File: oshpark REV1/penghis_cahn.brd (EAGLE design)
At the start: 99.4 x 99.6 mm, 67 parts, among them IC1 PCF8574T, P0 TPB1,27, P1 TPB1,27, T1 BC847, T2 BC847, U1 MCP73831

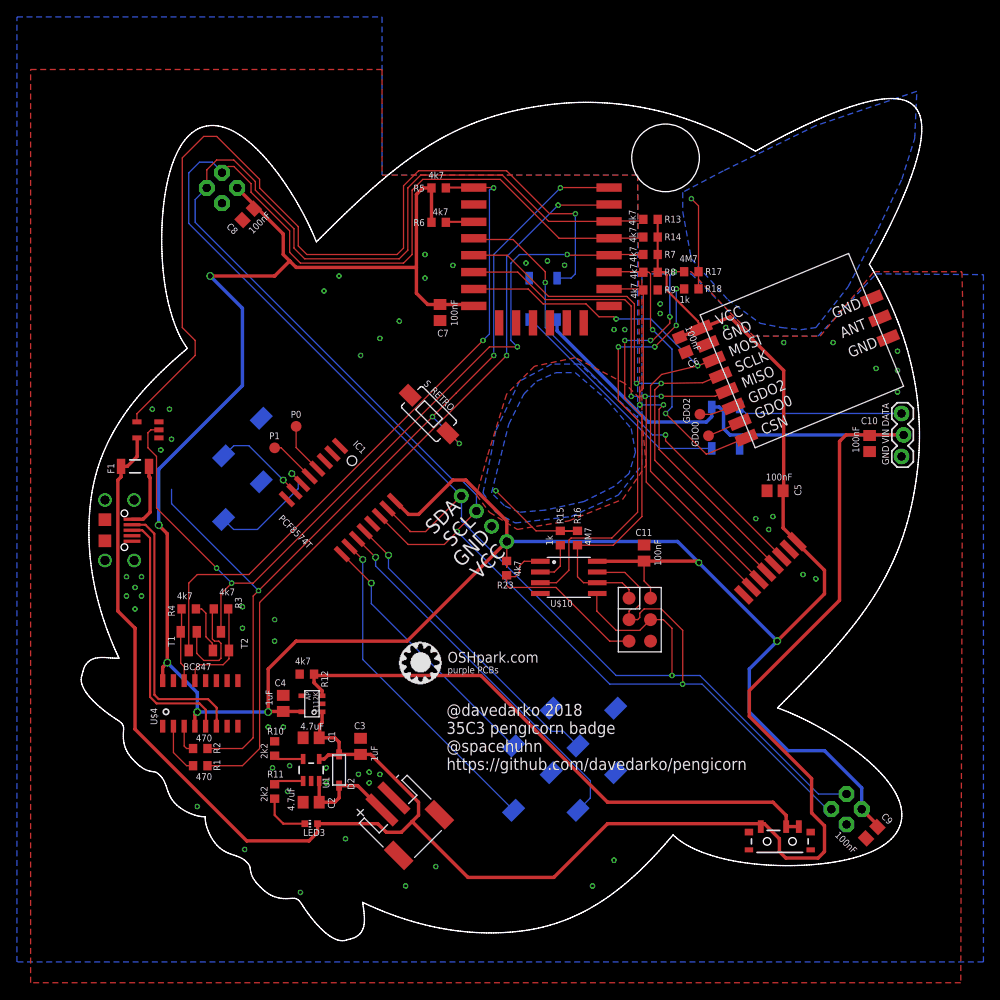
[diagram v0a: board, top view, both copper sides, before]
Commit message: minor updates
added TPS22918 for neopixels
updated labels
moved in nrf24 module
added SAO V1.69bis
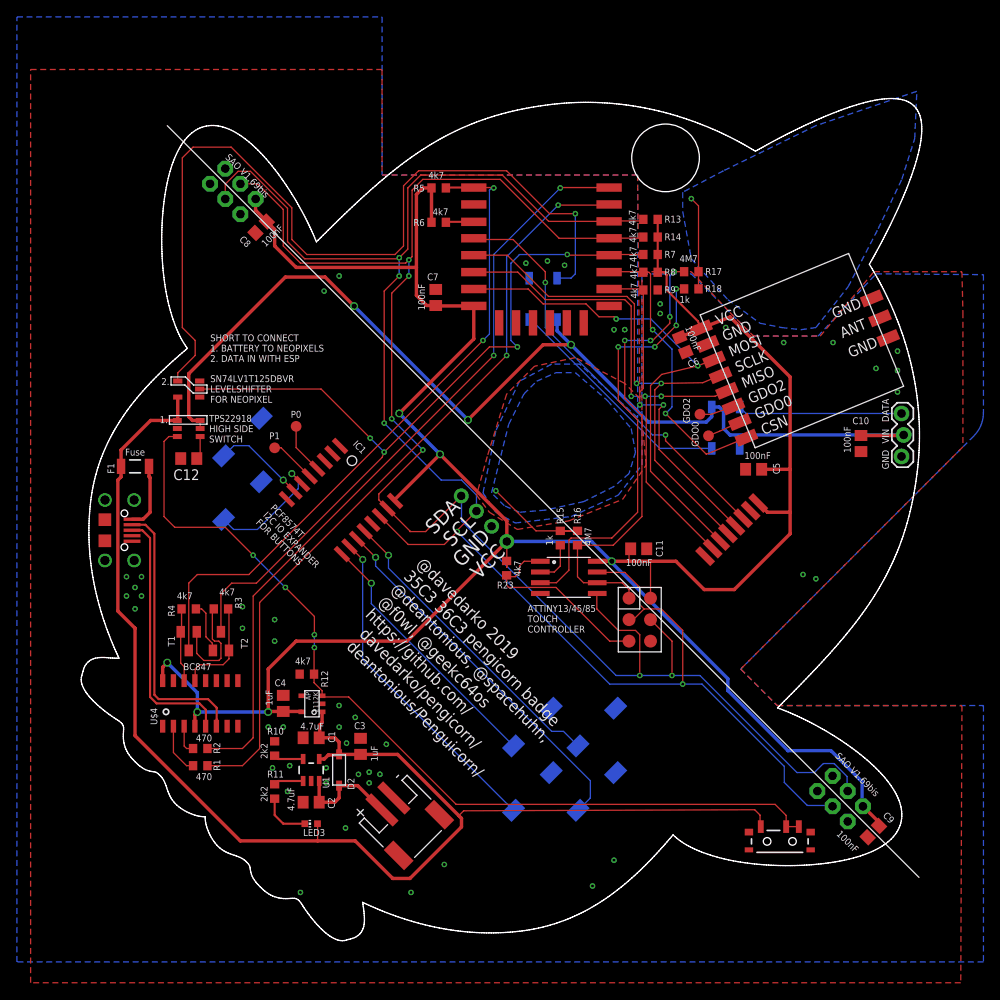
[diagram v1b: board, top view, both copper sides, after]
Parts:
- removed JP2, JP3: (no value), SparkFun-Connectors:2X2
- removed S_RETRO: SWITCH-MOMENTARY-2-SMD-1101NE, SparkFun-Electromechanical:TACTILE-SWITCH-1101NE
- added C12: 100nF, rcl:C0805
- added SAO1, SAO2: SAO-SHITTY-ADDONMASTER, SparkFun-Connectors:2X3-KEYED-FEMALE
- U$8: value OSHPARK_100MIL_TXT -> TPS22917; device LOGOS:OSHPARK_LOGO -> tps22917:SOT23
- moved U$8 45.7 mm to (12.7, 50.5)
- moved U$9 18.3 mm to (29.7, 30.2)
- moved U$5 6.82 mm to (12.7, 55.2)
- moved U$1 6.47 mm to (82.8, 32.7)
- moved C5 3.59 mm to (79.5, 45.7)
- moved C8 2.16 mm to (21.3, 74.3)
- moved C7 1.85 mm to (41.9, 66.0), turned to 90 degrees
- moved C10 1.02 mm to (92.2, 48.8)
- moved C11 0.81 mm to (65.9, 36.3), turned to 0 degrees
- moved C9 0.23 mm to (93.7, 2.88)
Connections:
- removed net N$9: R12.2, S1.1, S1.2, U$3.P$3
- new net N$16: C12.1, U$8.P$4
- new net NEO_POWER: C10.1, JP4.2, LED1.1-VDD, LED2.1-VDD, U$8.P$5, U$8.P$6
- new net V_EN: R12.2, S1.1, S1.2, U$3.P$3, U$8.P$3
- net ESP_TX: no longer S_RETRO.P$2
- net GND: now also C12.2, SAO1.6, SAO2.6, U$8.P$2; no longer JP2.3, JP3.3, S_RETRO.P$1
- net SCL_AVR_SCK: now also SAO1.4, SAO2.4; no longer JP2.4, JP3.4
- net SDA_AVR_MOSI: now also SAO1.3, SAO2.3; no longer JP2.2, JP3.2
- net VCC: now also SAO1.5, SAO2.5; no longer JP2.1, JP3.1
- net VIN: now also U$8.P$1; no longer C10.1, JP4.2, LED1.1-VDD, LED2.1-VDD
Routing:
- net NEO_POWER: track 0.00 -> 124.0 mm, vias 0 -> 3
- net VIN: track 274.3 -> 161.8 mm
- net V_EN: track 0.00 -> 106.7 mm, vias 0 -> 4
- net N$9: track 68.5 -> 0.00 mm
- net VCC: track 354.4 -> 313.4 mm, vias 7 -> 6
- net ESP_TX: track 114.4 -> 91.8 mm, vias 5 -> 2
- net SDA_AVR_MOSI: track 217.0 -> 196.3 mm, vias 1 -> 6
- net SCL_AVR_SCK: track 222.3 -> 202.0 mm, vias 2 -> 5
- net NEO_IN: track 110.0 -> 102.2 mm
- net ESP_SCLK: track 69.1 -> 62.6 mm
- net NRF_CE: track 56.3 -> 49.8 mm
- net ESP_MISO: track 70.3 -> 63.8 mm
- net NRF_CSN: track 45.4 -> 38.9 mm
- net ESP_MOSI: track 66.8 -> 60.4 mm
- net N$16: track 0.00 -> 2.77 mm
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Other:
- board text added: "1."
- board text added: "2."
- board text added: "@davedarko 2019 35C3 36C3 pengicorn badge @deantonious, @spacehuhn, @f0wl, @geekc64os https://github.com/ davedarko/pengicorn/ deantonious/Penguicorn/"
- board text added: "ATTINY13/45/85 TOUCH CONTROLLER"
- board text added: "Fuse"
- board text added: "PCF8574T I2C IO EXPANDER FOR BUTTONS"
- board text added: "SAO V1.69bis"
- board text added: "SHORT TO CONNECT 1. BATTERY TO NEOPIXELS 2. DATA IN WITH ESP"
- board text added: "SN74LV1T125DBVR LEVELSHIFTER FOR NEOPIXEL"
- board text added: "TPS22918 HIGH SIDE SWITCH"
- board text removed: "@davedarko 2018 35C3 pengicorn badge @spacehuhn https://github.com/davedarko/pengicorn"
